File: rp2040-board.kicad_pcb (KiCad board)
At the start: 4 copper layers, 105.3 x 75.1 mm, 161 parts, among them J1 24V IN, J10 E0-RUNOUT, J11 FAN0, J12 FAN1, J13 FAN2, J14 HB, J15 E0, J16 TH-E0, J17 X-STEPPER, J18 Y-STEPPER, J19 ZA-STEPPER, J2 USB4105-GF-A, J20 E0-STEPPER, J21 ZB-STEPPER, J22 Exp. Header 2, J23 Exp. Header 3, J3 PGA2040, J4 Exp. Header 1, J5 PROBE, J6 X-ENDSTOP, J7 TH-HB, J8 Y-ENDSTOP, J9 Z-ENDSTOP, Q1 AO3400C, Q2 AO3400C, Q3 AO3400C, U1 AMS1117-3.3, U2 TPS5450DDAR, U3 74HCT365D,653, U4 FDS8896, U5 FDS8896, U6 TMC2226-SA-T, U7 TMC2226-SA-T, U8 TMC2226-SA-T, U9 TMC2226-SA-T

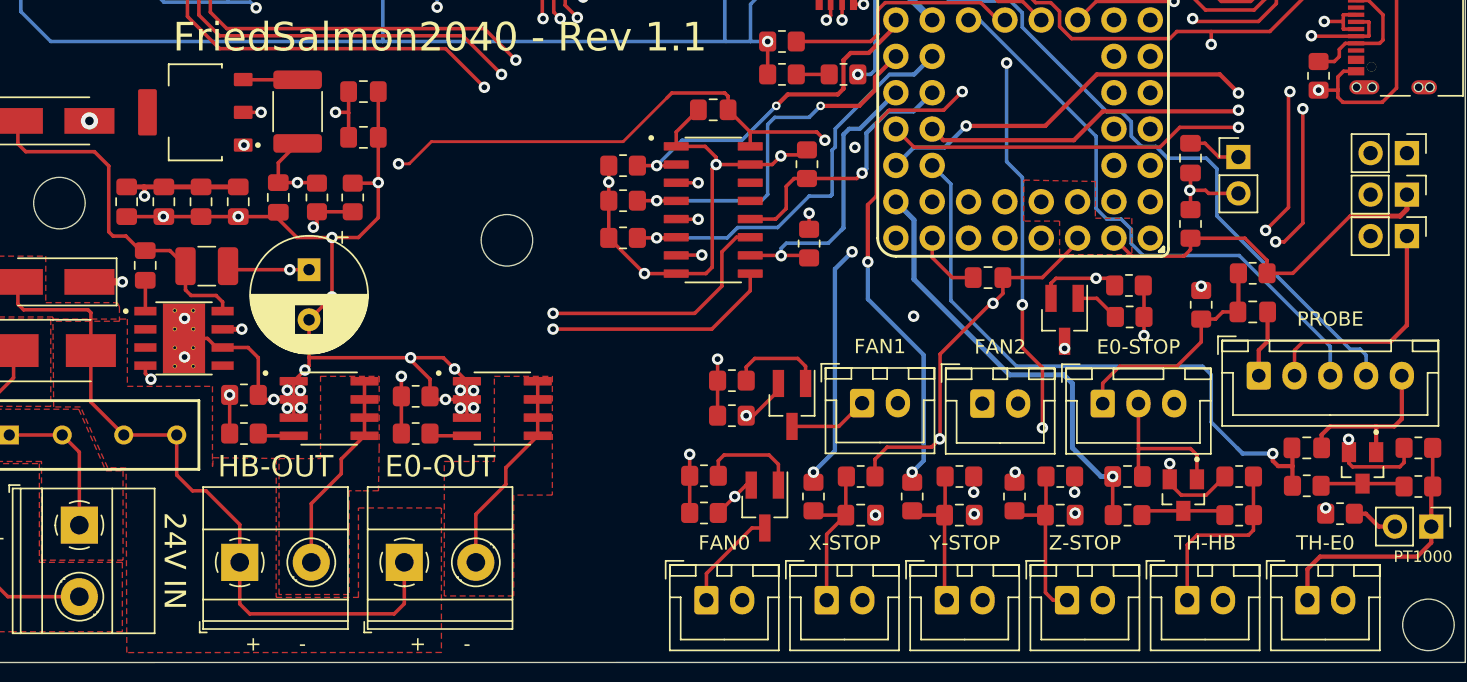
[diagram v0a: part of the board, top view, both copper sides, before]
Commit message: Update BOM + Minor PCB Touchups
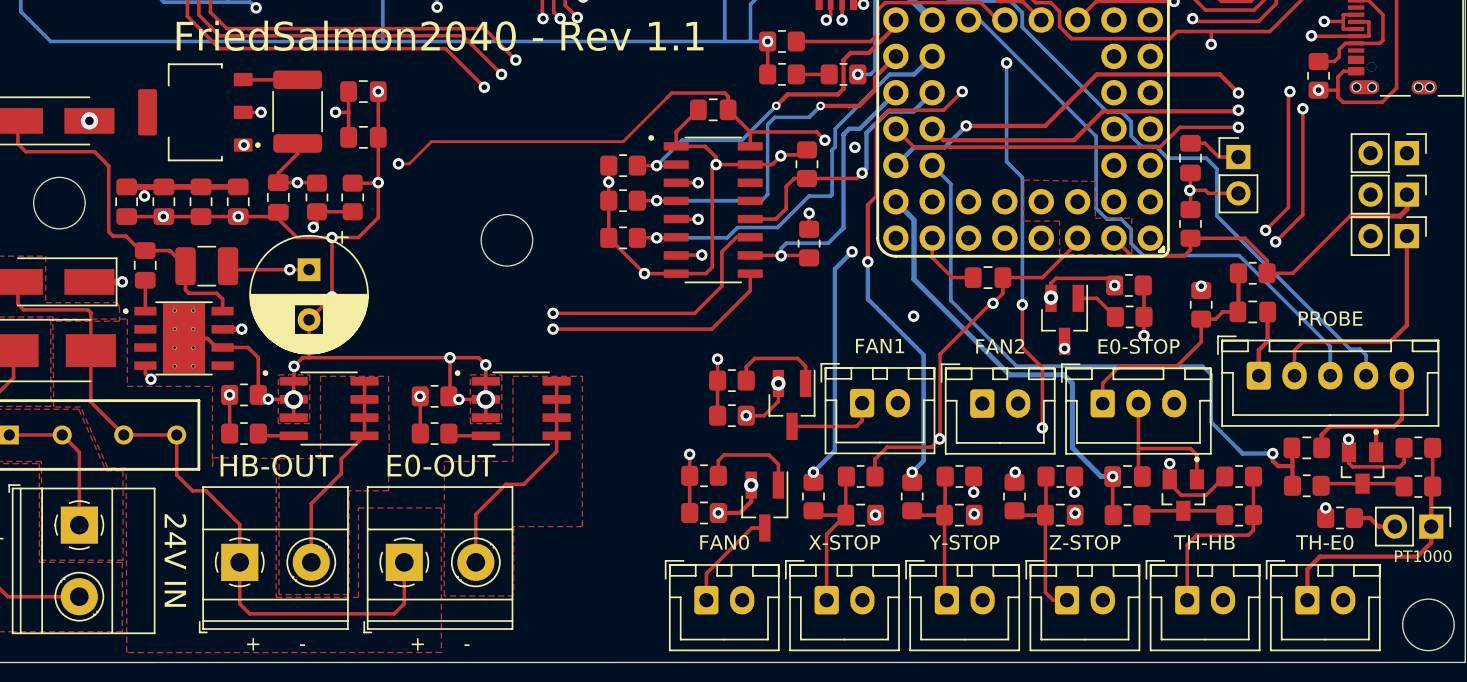
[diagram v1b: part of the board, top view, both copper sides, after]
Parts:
- F1: value 0.35A -> 0.7A
- moved R18 1.32 mm to (130.9, 122.1)
- moved R19 1.32 mm to (130.9, 119.5)
- moved U5 1.32 mm to (137.0, 120.3)
- moved R57 0.30 mm to (194.2, 128.0)
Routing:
- net GND: track 237.5 -> 239.1 mm, vias 47 -> 43
- net Net-(J15-Pad2): track 14.4 -> 15.7 mm
- net Net-(J12-Pad1): track 5.57 -> 6.29 mm
- added copper zone on F.Cu, net GND

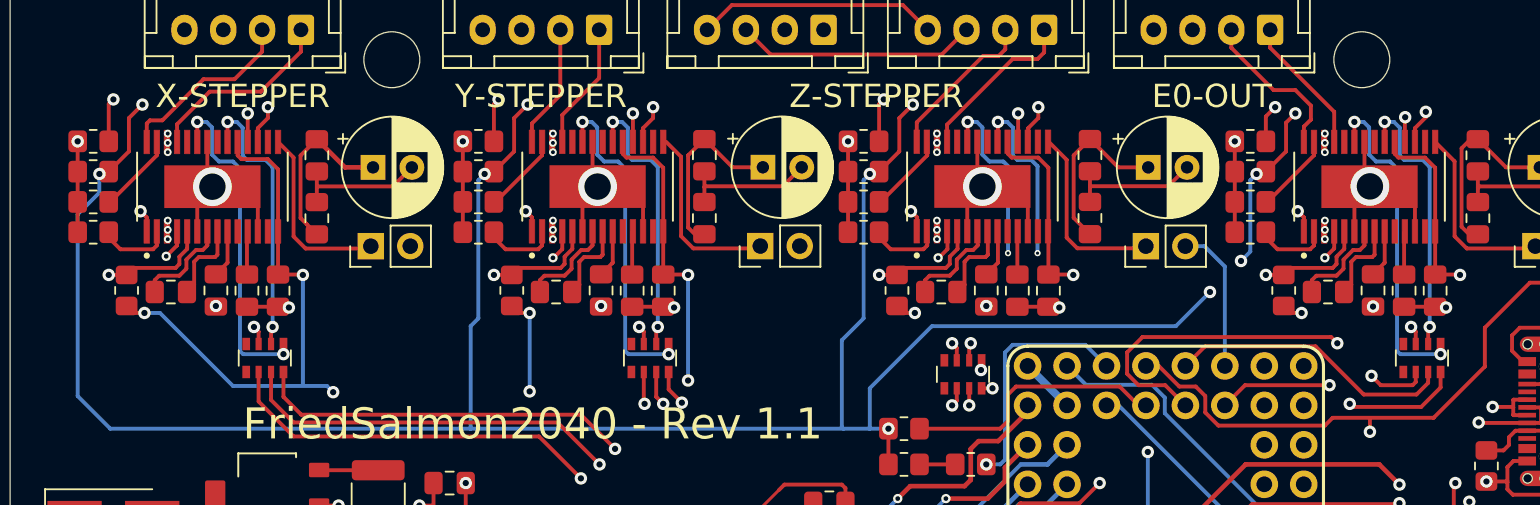
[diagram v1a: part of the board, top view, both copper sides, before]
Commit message: Fix driver UART address configuration
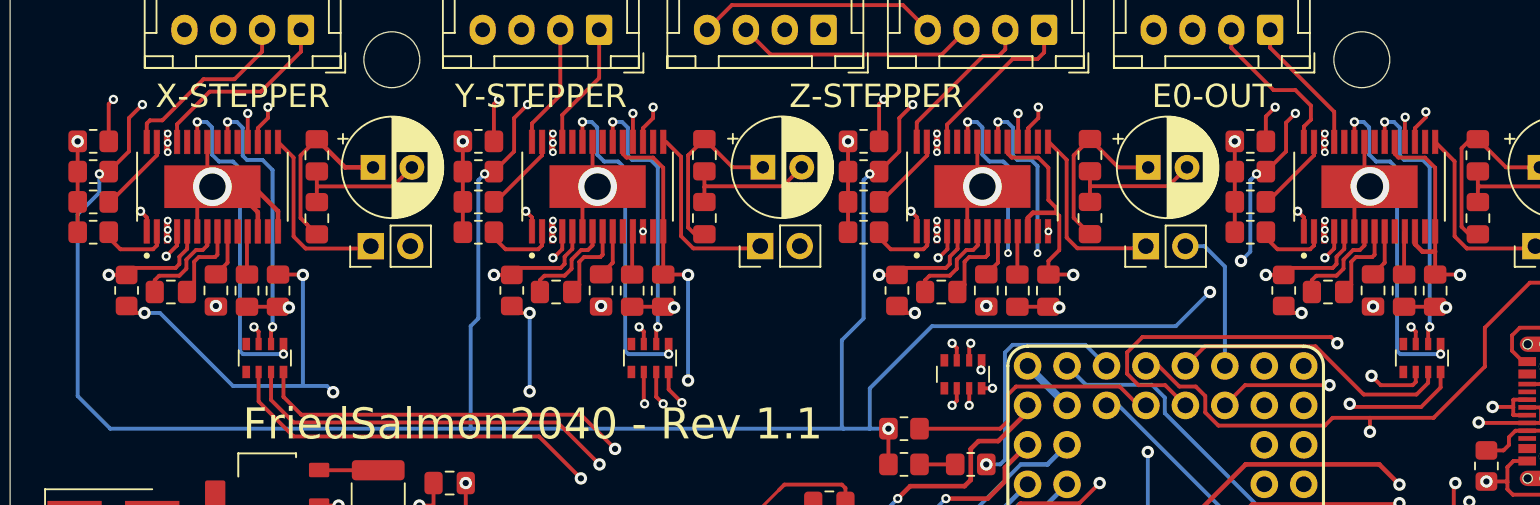
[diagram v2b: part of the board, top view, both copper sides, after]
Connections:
- U6 pad 14: +3.3V -> GND
- U8 pad 12: GND -> +3.3V
- U9 pad 12: GND -> +3.3V
- U9 pad 14: +3.3V -> GND
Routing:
- net +3.3V: track 359.9 -> 355.3 mm
- net GND: track 239.1 -> 243.0 mm, vias 43 -> 45

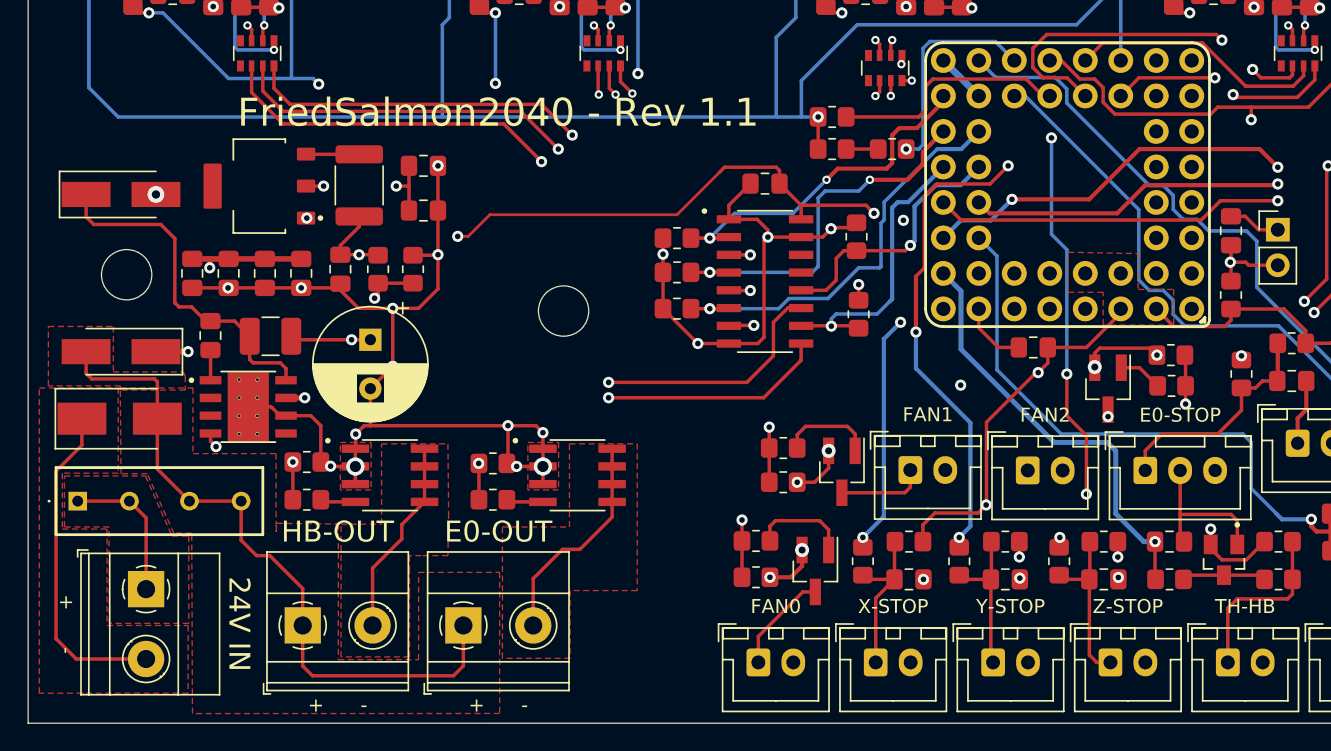
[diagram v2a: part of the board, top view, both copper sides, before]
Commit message: add fan diodes + cleanup + copper fill clearances
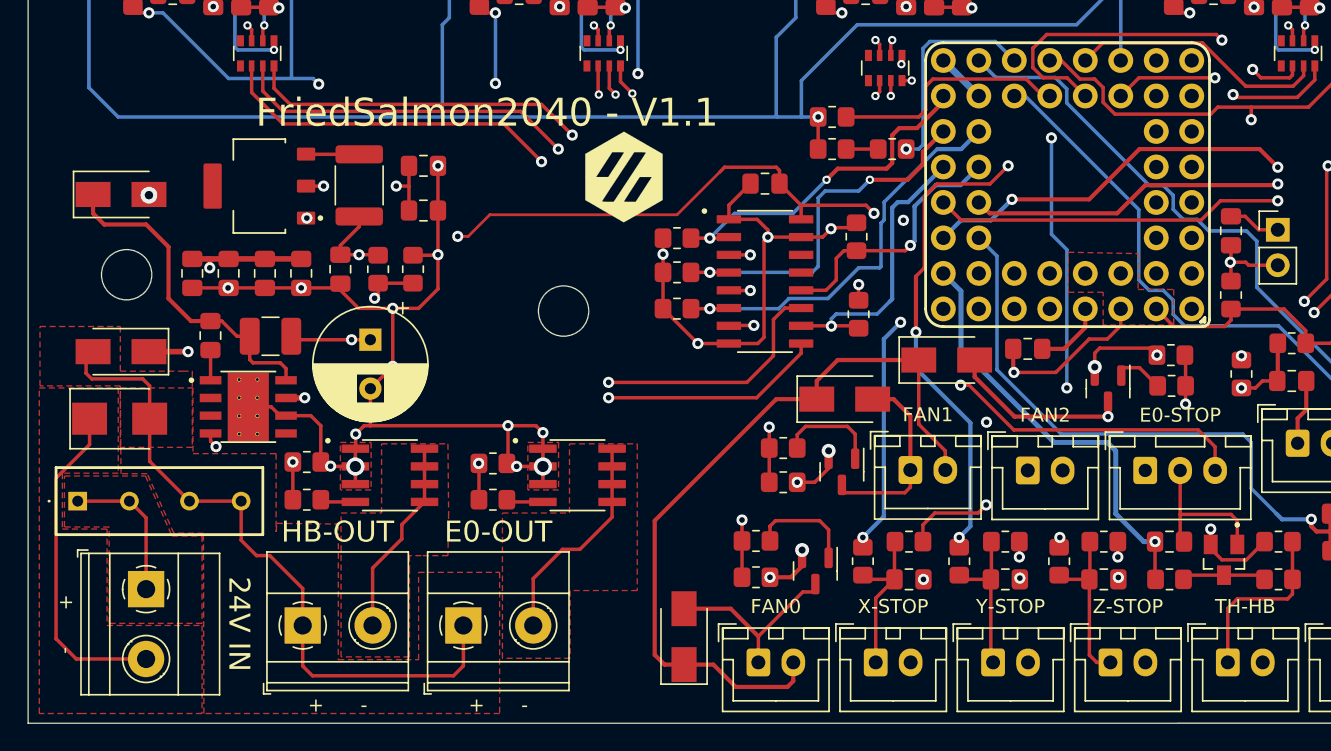
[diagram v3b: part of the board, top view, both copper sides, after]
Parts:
- added D6: S1A, Diode_SMD:D_SMA, F.Cu at (144.6, 131.9)
- added D7: S1A, Diode_SMD:D_SMA, F.Cu at (156.1, 114.9)
- added D8: S1A, Diode_SMD:D_SMA, F.Cu at (163.4, 112.1)
- added G***: LOGO, TRA_KiCad_Footprints:VoronLogo_6pt5mm_silkScreen, F.Cu at (140.3, 99.0)
- D1, D3: footprint Diode_SMD:D_SMA_Handsoldering -> Diode_SMD:D_SMA
- D2: footprint Diode_SMD:D_SMB_Handsoldering -> Diode_SMD:D_SMB
- Q1, Q2, Q3: footprint Package_TO_SOT_SMD:SOT-23_Handsoldering -> Package_TO_SOT_SMD:SOT-23
- moved C7 0.41 mm to (169.2, 111.3), turned to 180 degrees
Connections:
- J3 pad A4: Net-(C5-Pad2) -> Net-(C7-Pad1)
- J3 pad A7: Net-(C7-Pad1) -> Net-(C5-Pad2)
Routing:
- net VCC: track 155.3 -> 209.9 mm
- net Net-(D8-Pad2): track 9.08 -> 21.0 mm
- net Net-(D7-Pad2): track 6.29 -> 13.4 mm
- net Net-(D6-Pad2): track 7.26 -> 13.4 mm
- net Net-(C5-Pad2): track 21.0 -> 26.7 mm
- net Net-(C9-Pad2): track 24.6 -> 23.7 mm
- net +3.3V: track 355.3 -> 356.1 mm, vias 20 -> 21
- net Net-(C7-Pad1): track 4.70 -> 5.20 mm
- net ZSTOP: vias 4 -> 3
- net Net-(C17-Pad1): vias 0 -> 1
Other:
- board text added: "FriedSalmon2040 - V1.1"
- board text removed: "FriedSalmon2040 - Rev 1.1"

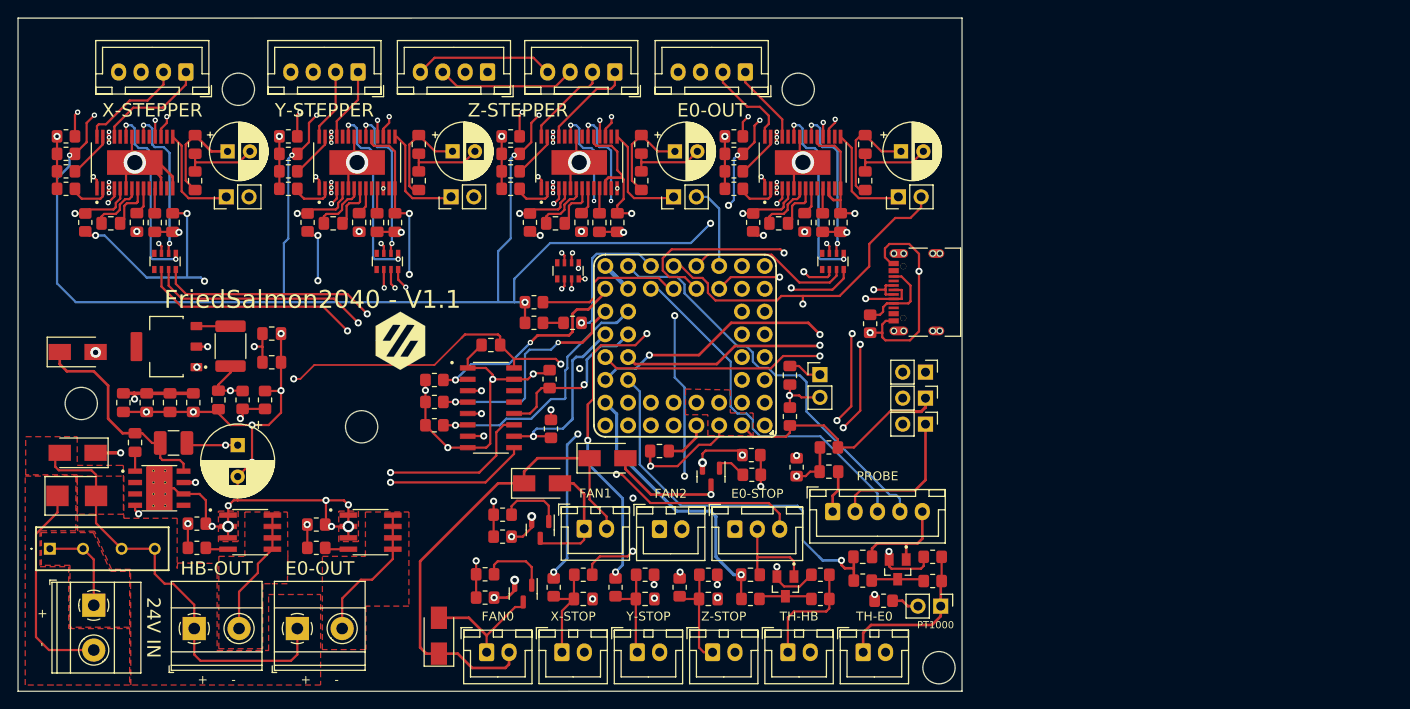
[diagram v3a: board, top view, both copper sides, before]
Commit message: Big updates, start of V2, actual RP2040
change from V1.2 to V2 because of many optimizations to come
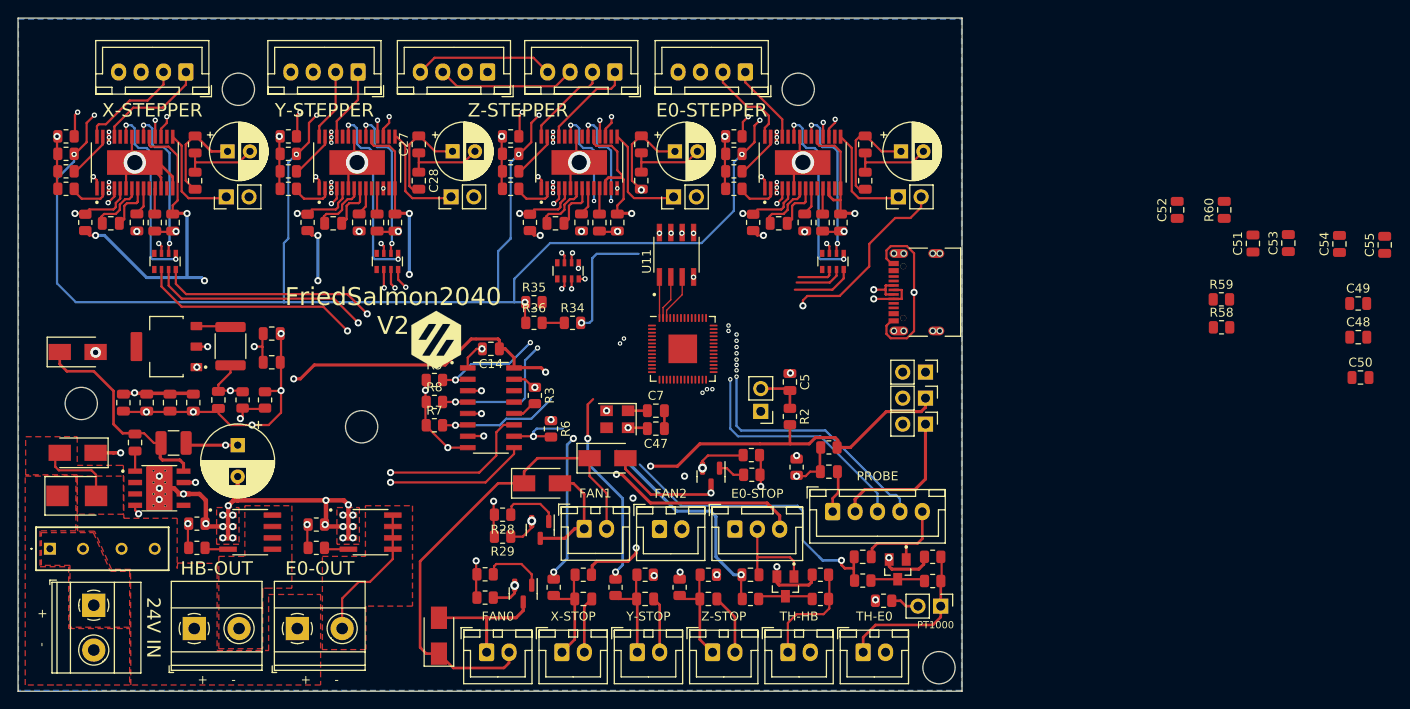
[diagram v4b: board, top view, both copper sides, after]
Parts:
- removed J3: PGA2040, PGA2040:PGA2040_PTH_NO_SLOT
- removed R1: 5.1K, Resistor_SMD:R_0805_2012Metric_Pad1.20x1.40mm_HandSolder
- added C47: 10pF, Capacitor_SMD:C_0805_2012Metric, F.Cu at (168.8, 108.8)
- added C48: 2.2uF, Capacitor_SMD:C_0805_2012Metric, F.Cu at (247.2, 98.6)
- added C49: 0.1uF, Capacitor_SMD:C_0805_2012Metric, F.Cu at (247.1, 94.8)
- added C50: 0.1uF, Capacitor_SMD:C_0805_2012Metric, F.Cu at (247.4, 103.1)
- added C51: 2.2uF, Capacitor_SMD:C_0805_2012Metric, F.Cu at (235.4, 88.2)
- added C52: 2.2uF, Capacitor_SMD:C_0805_2012Metric, F.Cu at (226.9, 84.4)
- added C53: 0.1uF, Capacitor_SMD:C_0805_2012Metric, F.Cu at (239.3, 88.1)
- added C54: 0.1uF, Capacitor_SMD:C_0805_2012Metric, F.Cu at (245.1, 88.2)
- added C55: 0.1uF, Capacitor_SMD:C_0805_2012Metric, F.Cu at (250.1, 88.3)
- added R58: 22R, Resistor_SMD:R_0805_2012Metric, F.Cu at (231.9, 97.5)
- added R59: 22R, Resistor_SMD:R_0805_2012Metric, F.Cu at (231.9, 94.4)
- added R60: 200R, Capacitor_SMD:C_0805_2012Metric, F.Cu at (232.2, 84.4)
- added U10: RP2040, Package_DFN_QFN:QFN-56-1EP_7x7mm_P0.4mm_EP3.2x3.2mm, F.Cu at (171.8, 99.9)
- added U11: W25Q80DVSNIG, FDS8896:SOIC127P600X175-8N, F.Cu at (171.1, 89.4)
- added Y1: 12MHz, Oscillator:Oscillator_SMD_SeikoEpson_SG8002CE-4Pin_3.2x2.5mm, F.Cu at (164.5, 107.8)
- C1, C10, C12, C13, C14, C15, C16, C17, C18, C19, C2, C20, C21, C22, C23, C24, C25, C26, C27, C28, C29, C3, C30, C33, C34, C35, C36, C37, C38, C39, C4, C40, C41, C42, C43, C44, C5, C6, C8, C9: footprint Capacitor_SMD:C_0805_2012Metric_Pad1.18x1.45mm_HandSolder -> Capacitor_SMD:C_0805_2012Metric
- C7: value 0.1uF -> 10pF; footprint Capacitor_SMD:C_0805_2012Metric_Pad1.18x1.45mm_HandSolder -> Capacitor_SMD:C_0805_2012Metric
- F1: footprint Fuse:Fuse_1812_4532Metric_Pad1.30x3.40mm_HandSolder -> Fuse:Fuse_1812_4532Metric
- L1: footprint Inductor_SMD:L_1210_3225Metric_Pad1.42x2.65mm_HandSolder -> Inductor_SMD:L_1210_3225Metric
- R10, R11, R12, R13, R14, R15, R16, R17, R18, R19, R2, R20, R21, R22, R23, R24, R25, R26, R27, R28, R29, R3, R30, R31, R32, R33, R34, R35, R36, R37, R38, R39, R4, R40, R41, R42, R43, R44, R45, R46, R47, R48, R49, R5, R50, R51, R52, R53, R54, R55, R56, R57, R6, R7, R8, R9: footprint Resistor_SMD:R_0805_2012Metric_Pad1.20x1.40mm_HandSolder -> Resistor_SMD:R_0805_2012Metric
- moved JP1 7.77 mm to (180.5, 106.9), turned to 180 degrees
- moved C7 4.52 mm to (168.8, 106.8), turned to 0 degrees
- moved G*** 4.00 mm to (144.3, 98.9)
- moved R3 2.46 mm to (155.3, 105.1)
- moved C5 0.75 mm to (183.8, 103.6)
- moved C14 0.43 mm to (150.4, 99.9)
- turned R2 to -90 degrees
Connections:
- net Net-(J2-PadA6) renamed D+
- net Net-(J2-PadA7) renamed D-
- C7 pad 2: +3.3V -> Net-(C47-Pad1)
- J2 pad A5: Net-(J2-PadA5) -> unconnected-(J2-PadA5)
- J2 pad B5: Net-(J2-PadA5) -> unconnected-(J2-PadB5)
- R2 pad 1: +3.3V -> Net-(C5-Pad2)
- R2 pad 2: Net-(C5-Pad2) -> +3.3V
- RN2 pad 5: YSTP -> unconnected-(RN2-Pad5)
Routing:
- net XSTP: track 75.0 -> 24.7 mm
- net XEN: track 74.6 -> 24.7 mm, vias 2 -> 1
- net YSTP: track 47.6 -> 0.00 mm, vias 1 -> 0
- net XDIR: track 69.9 -> 24.3 mm
- net D+: track 43.9 -> 4.11 mm, vias 3 -> 1
- net D-: track 44.1 -> 4.99 mm, vias 3 -> 1
- net VCC: track 209.9 -> 174.8 mm, vias 28 -> 30
- net YSTOP: track 77.4 -> 42.9 mm, vias 3 -> 2
- net ZSTOP: track 48.9 -> 15.2 mm, vias 3 -> 2
- net unconnected-(RN2-Pad5): track 0.00 -> 25.8 mm, vias 0 -> 1
- net E0DIR: track 31.8 -> 6.97 mm, vias 2 -> 0
- net ZSTP: track 25.2 -> 1.10 mm
- net Net-(D2-Pad1): track 23.8 -> 0.00 mm
- net YDIR: track 42.0 -> 20.2 mm
- net ZEN: track 22.7 -> 1.22 mm
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- added copper zone on B.Cu, net Net-(D2-Pad1)
- added copper zone on In1.Cu, net Net-(D2-Pad1)
- added copper zone on In2.Cu, net Net-(D2-Pad1)
- removed copper zone on F.Cu, net +3.3V
- removed copper zone on In1.Cu, net GND
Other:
- board text added: "E0-STEPPER"
- board text added: "FriedSalmon2040 V2"
- board text removed: "(PK is a bad influence) Party in the back!"
- board text removed: "FriedSalmon2040 - V1.1"
